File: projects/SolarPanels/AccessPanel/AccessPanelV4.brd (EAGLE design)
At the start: 99 x 85.1 mm, 39 parts

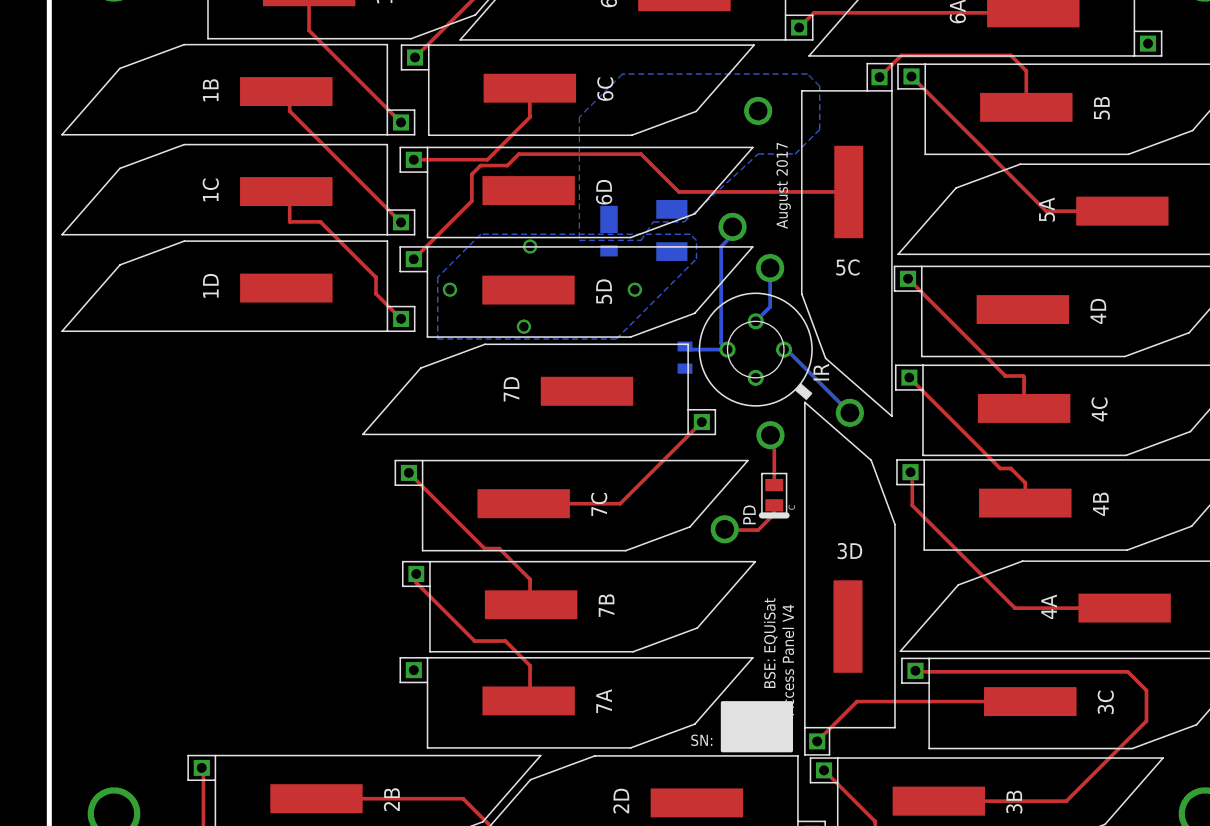
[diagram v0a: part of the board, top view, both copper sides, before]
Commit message: Additional edits to Access Panel V4 layout. Just needs the access connector.
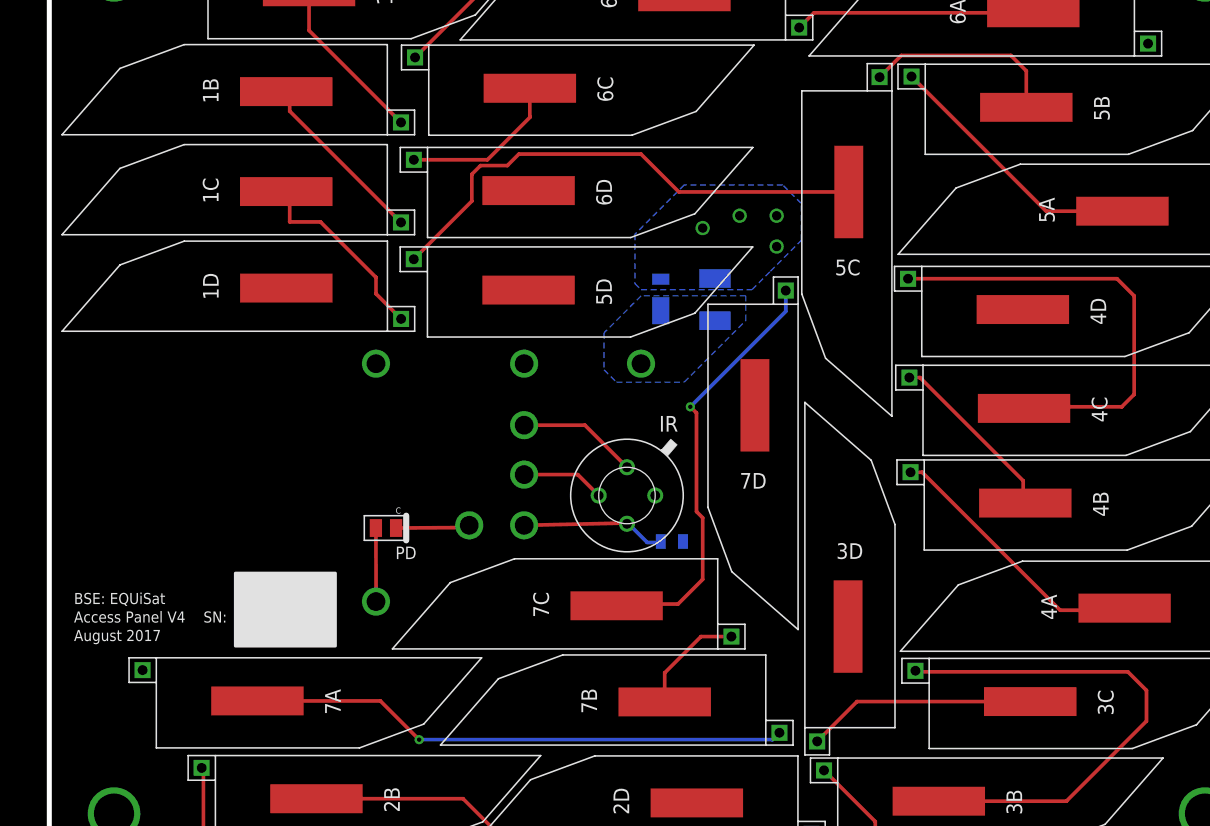
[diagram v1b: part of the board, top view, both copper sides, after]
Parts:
- added V2, V5: GND, BrownSpaceEngineering:VIA-60MIL
- moved V4 34.7 mm to (17.5, 30.7)
- moved PD 32.0 mm to (18.3, 37.1), turned to 180 degrees
- moved V3 29.5 mm to (29.5, 36.9), turned to 270 degrees
- moved SCL 26.4 mm to (29.5, 45.0)
- moved SDA 26.1 mm to (29.5, 41.0)
- moved V1 22.6 mm to (39.0, 50.0)
- moved 7A 22.0 mm to (12.1, 23.6)
- moved V6 20.7 mm to (25.1, 36.9), turned to 90 degrees
- moved 7D 19.3 mm to (49.2, 42.4), turned to 90 degrees
- moved IR 15.8 mm to (37.9, 39.3), turned to 90 degrees
- moved C1 15.0 mm to (41.5, 35.6), turned to 0 degrees
- moved 7C 10.2 mm to (32.8, 29.4), turned to 0 degrees
- moved 7B 10.1 mm to (36.7, 21.6), turned to 0 degrees
- moved D1 6.68 mm to (40.6, 55.4), turned to 90 degrees
- moved R1 6.60 mm to (45.0, 55.2), turned to 270 degrees
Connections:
- net GND: now also V2.P$1, V5.P$1
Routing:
- net N$23: track 15.6 -> 43.9 mm, vias 0 -> 1
- net N$5: track 15.3 -> 36.5 mm
- net N$22: track 17.2 -> 34.9 mm, vias 0 -> 1
- net N$24: track 15.5 -> 8.99 mm
- net 3V3-IR: track 14.1 -> 11.8 mm
- net SCL: track 7.47 -> 9.75 mm
- net SDA: track 4.80 -> 6.75 mm
- net GND: track 4.36 -> 5.97 mm
- net N$11: track 23.4 -> 22.1 mm
- net PD-OUT: track 5.29 -> 6.11 mm

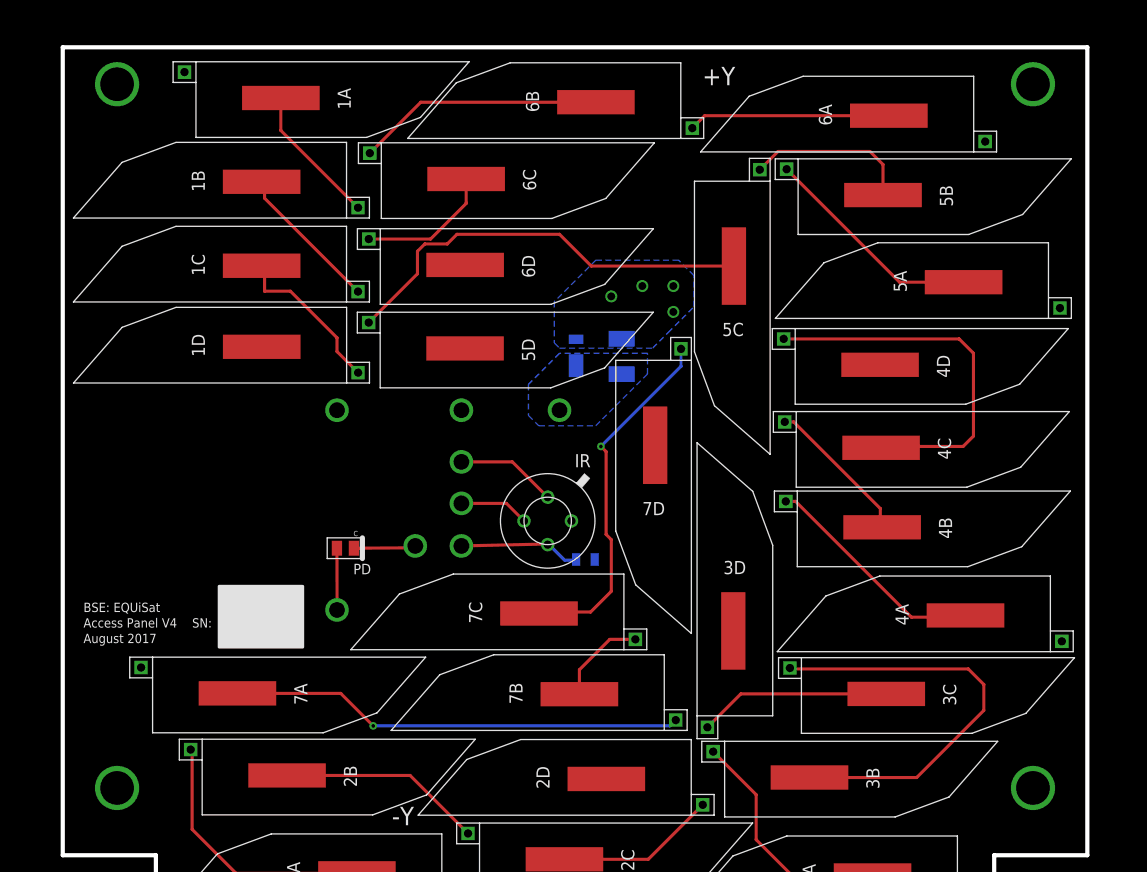
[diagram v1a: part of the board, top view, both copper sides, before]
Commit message: Added new access panel connector and completed AccessPanelV4.
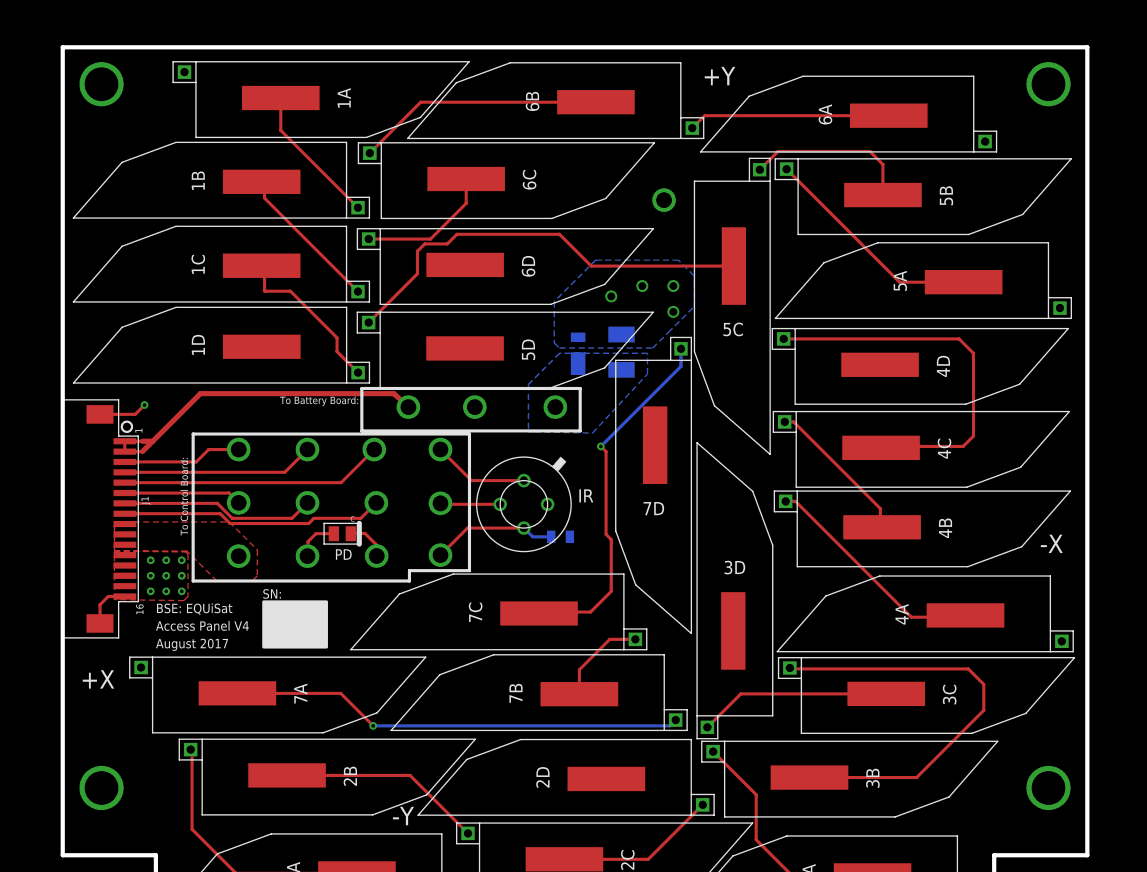
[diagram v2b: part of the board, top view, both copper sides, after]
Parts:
- added J1: FFC-16, BrownSpaceEngineering:68611614422
- added V10: SWDCLK, BrownSpaceEngineering:VIA-60MIL
- added V11: RESETN, BrownSpaceEngineering:VIA-60MIL
- added V14: USART_RX, BrownSpaceEngineering:VIA-60MIL
- added V15: USART_TX, BrownSpaceEngineering:VIA-60MIL
- added V16: 3V3, BrownSpaceEngineering:VIA-60MIL
- added V7: UMB-CHG, BrownSpaceEngineering:VIA-60MIL
- added V8: VIN-EXT, BrownSpaceEngineering:VIA-60MIL
- added V9: SWDIO, BrownSpaceEngineering:VIA-60MIL
- moved V4 50.7 mm to (49.1, 70.3)
- moved V5 14.4 mm to (14.7, 35.9), turned to 180 degrees
- moved V6 3.85 mm to (21.3, 35.9), turned to 180 degrees
- moved C1 3.26 mm to (39.1, 37.8)
- moved IR 2.80 mm to (35.6, 40.9)
- moved SCL 2.34 mm to (27.5, 46.2), turned to 180 degrees
- moved V3 2.20 mm to (27.5, 36.0), turned to 0 degrees
- moved SDA 2.02 mm to (27.5, 41.0), turned to 180 degrees
- moved PD 1.43 mm to (18.0, 38.5)
- moved V2 1.33 mm to (30.8, 50.3)
- moved V1 0.50 mm to (38.6, 50.3)
- moved R1 0.40 mm to (45.0, 55.6)
- moved D1 0.28 mm to (40.8, 55.6)
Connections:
- new net 3V3: J1.P$8, V16.P$1
- new net RESETN: J1.P$5, V11.P$1
- new net SWDCLK: J1.P$6, V10.P$1
- new net SWDIO: J1.P$7, V9.P$1
- new net UMB-CHG: J1.P$1, J1.P$2, V7.P$1
- new net USART_RX: J1.P$4, V14.P$1
- new net USART_TX: J1.P$3, V15.P$1
- new net VIN-EXT: J1.P$10, J1.P$11, J1.P$9, V8.P$1
- net GND: now also J1.P$12, J1.P$13, J1.P$14, J1.P$15, J1.P$16, J1.P$17, J1.P$18
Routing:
- net UMB-CHG: track 0.00 -> 33.9 mm
- net 3V3: track 0.00 -> 25.5 mm
- net RESETN: track 0.00 -> 25.4 mm
- net SWDIO: track 0.00 -> 18.9 mm
- net USART_RX: track 0.00 -> 18.6 mm
- net USART_TX: track 0.00 -> 11.5 mm
- net SWDCLK: track 0.00 -> 11.4 mm
- net GND: track 5.97 -> 13.5 mm, vias 4 -> 14
- net PD-OUT: track 6.11 -> 4.04 mm
- net SDA: track 6.75 -> 5.80 mm
- added copper zone on layer 1, net GND
- added copper zone on layer 1, net VIN-EXT
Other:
- board text added: "+X"
- board text added: "-X"
- board text added: "To Battery Board:"
- board text added: "To Control Board:"

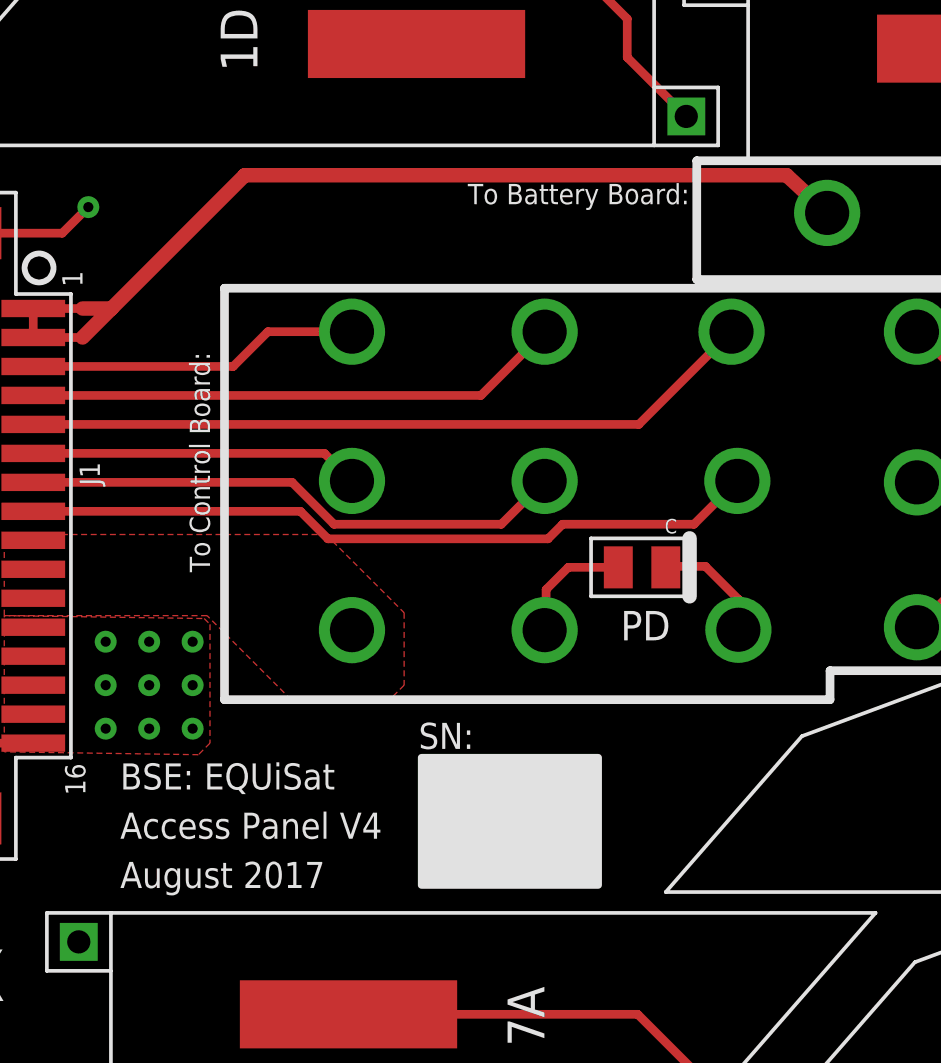
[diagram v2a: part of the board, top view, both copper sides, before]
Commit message: Added RBF switches to library. (changed ABF to RBF) Added RBF switches and routing to RBF Panel. Vectorized all text on solar panel boards and rearranged as needed.
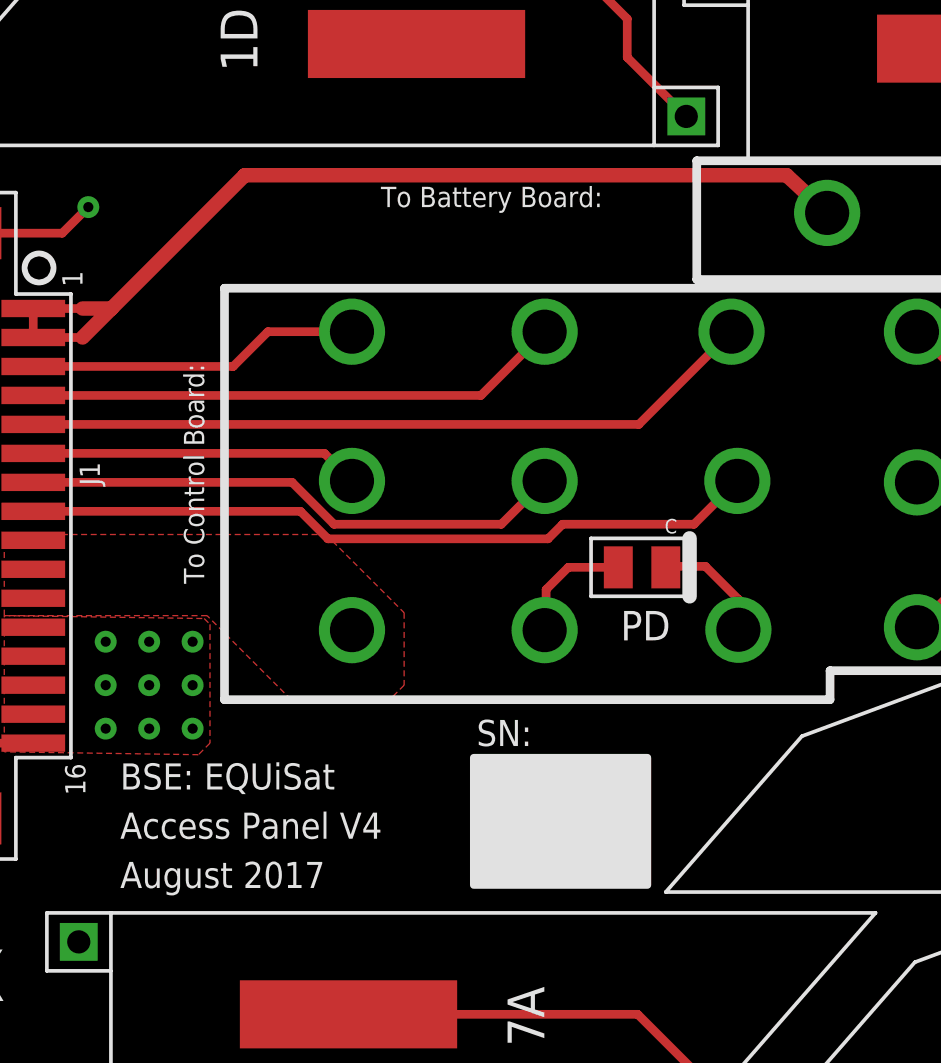
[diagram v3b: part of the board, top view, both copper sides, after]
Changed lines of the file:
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@@
 <drawing>
 <settings>
-<setting alwaysvectorfont="no"/>
+<setting alwaysvectorfont="yes"/>
 <setting verticaltext="up"/>
 </settings>
@@
 </polygon>
 <polygon width="0.254" layer="21">
-<vertex x="10.4" y="31.5"/>
-<vertex x="16.5" y="31.5"/>
-<vertex x="16.5" y="27.1"/>
-<vertex x="10.4" y="27.1"/>
+<vertex x="12.2" y="31.5"/>
+<vertex x="18.2" y="31.5"/>
+<vertex x="18.2" y="27.1"/>
+<vertex x="12.2" y="27.1"/>
 </polygon>
 <polygon width="0.254" layer="22">
@@
 <text x="0" y="30.4" size="0.9" layer="25">BSE: EQUiSat</text>
 <text x="0" y="28.7" size="0.9" layer="25">Access Panel V4</text>
-<text x="10.3" y="31.8" size="0.9" layer="25">SN:</text>
+<text x="12.3" y="31.9" size="0.9" layer="25">SN:</text>
 <text x="0" y="27" size="0.9" layer="25">August 2017</text>
-<text x="48.8" y="72.9" size="1.778" layer="26" rot="MR0">+Y</text>
+<text x="48.5" y="75.5" size="1.778" layer="26" rot="MR0">+Y</text>
 <text x="22.8" y="9.9" size="1.778" layer="25">-Y</text>
 <text x="40.3" y="8.9" size="1.778" layer="26" rot="MR0">-Y</text>
-<text x="43" y="74" size="0.9" layer="26" rot="MR0">Brown Space Engineering: EQUiSat</text>
-<text x="43" y="72" size="0.9" layer="26" rot="MR0">Access Panel V4</text>
-<text x="43" y="70" size="0.9" layer="26" rot="MR0">August 2017</text>
+<text x="44.9" y="72.9" size="0.9" layer="26" rot="MR0">Brown Space Engineering: EQUiSat</text>
+<text x="45" y="71.4" size="0.9" layer="26" rot="MR0">Access Panel V4</text>
+<text x="45" y="69.8" size="0.9" layer="26" rot="MR0">August 2017</text>
 <text x="43" y="67" size="0.9" layer="26" rot="MR0">SN:</text>
 <wire x1="3.6" y1="33.5" x2="24.5" y2="33.5" width="0.3" layer="21"/>
@@
 <wire x1="41" y1="48" x2="19.9" y2="48" width="0.3" layer="21"/>
 <wire x1="19.9" y1="48" x2="19.9" y2="52.1" width="0.3" layer="21"/>
-<text x="3.1" y="37.9" size="0.7" layer="21" rot="R90">To Control Board:</text>
-<text x="12" y="50.6" size="0.7" layer="21">To Battery Board:</text>
+<text x="2.9" y="37.5" size="0.7" layer="21" rot="R90">To Control Board:</text>
+<text x="9" y="50.5" size="0.7" layer="21">To Battery Board:</text>
 <text x="34.5" y="53" size="0.7" layer="22" rot="MR0">To Battery Board:</text>
 <text x="3" y="45.1" size="0.7" layer="22" rot="MR270">To Control Board:</text>
